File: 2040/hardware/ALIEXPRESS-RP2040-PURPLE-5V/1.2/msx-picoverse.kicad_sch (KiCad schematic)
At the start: 24 parts, among them Q1 BSS138, Q2 BSS138, Q3 BSS138, Q4 BSS138, Q5 BSS138, U1 RP2040-PURPLE

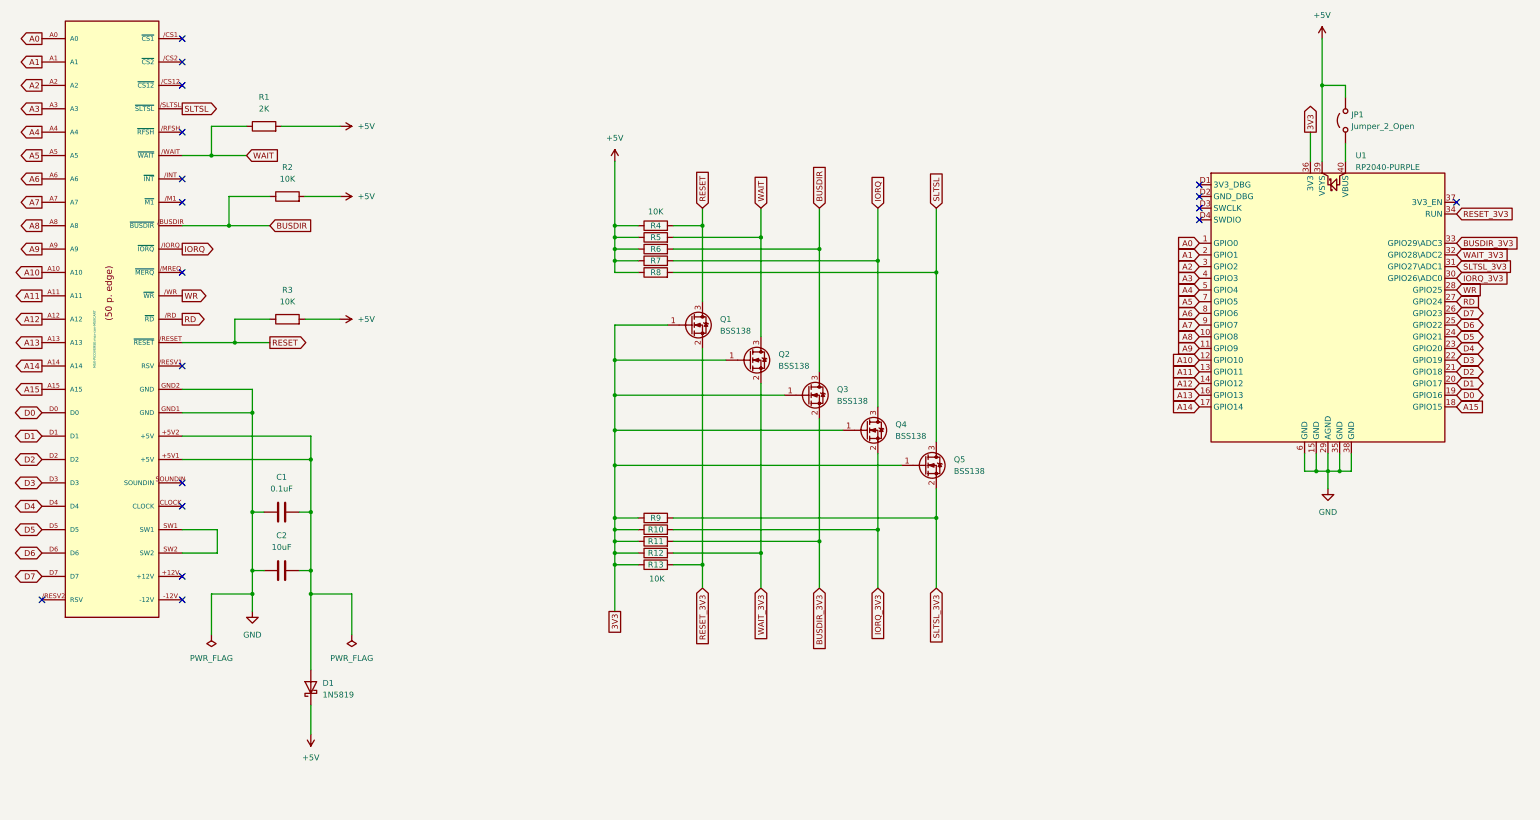
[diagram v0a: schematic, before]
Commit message: WiFi implementation for the 2040
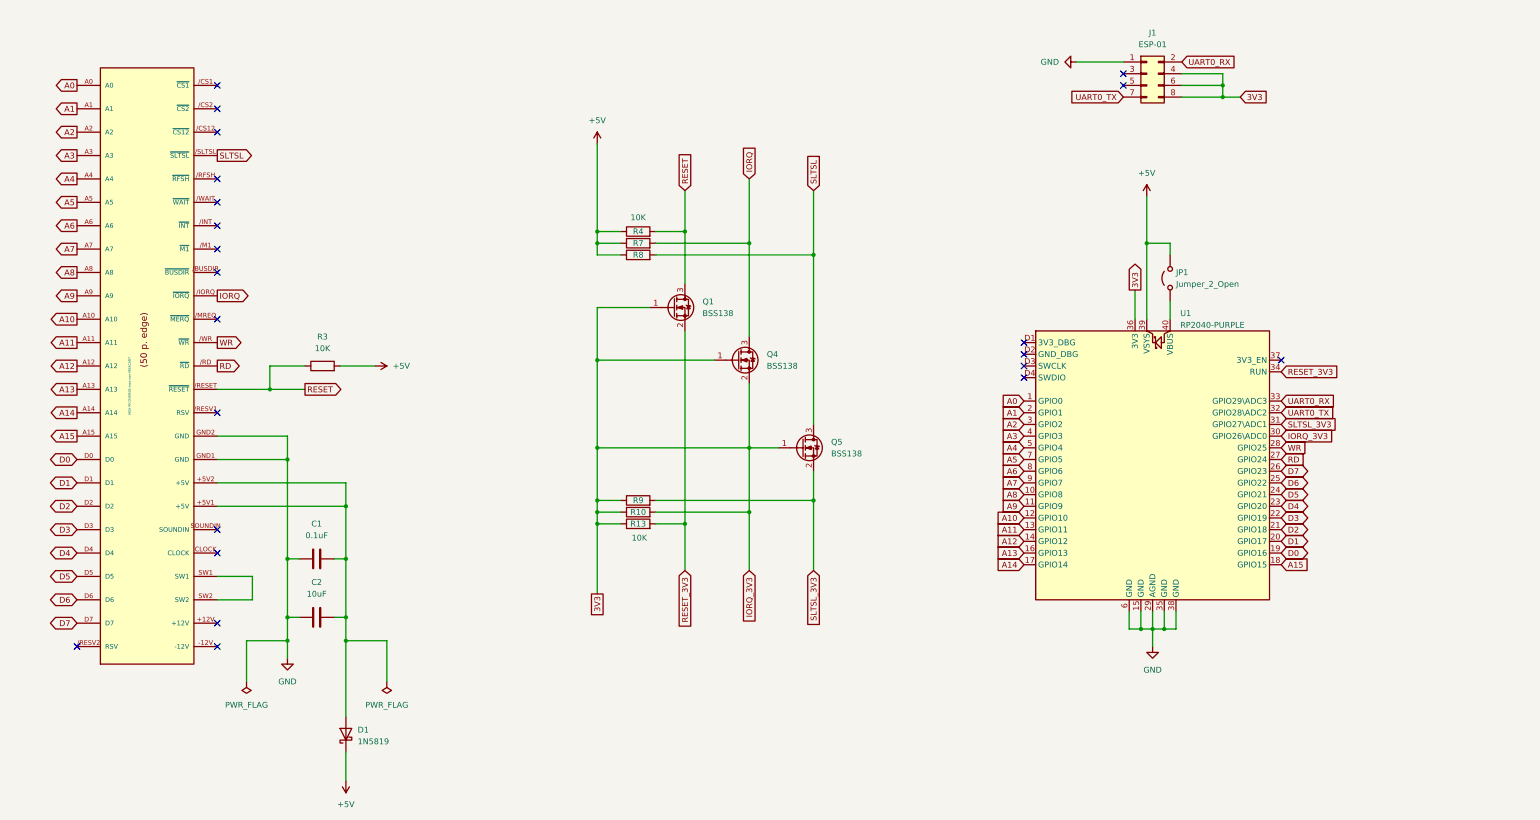
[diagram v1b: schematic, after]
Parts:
- removed Q2, Q3: BSS138, Package_TO_SOT_SMD:SOT-23, symbol Transistor_FET:BSS138
- removed R1: 2K, Resistor_SMD:R_0603_1608Metric_Pad0.98x0.95mm_HandSolder, symbol Device:R
- removed R11, R12, R2, R5, R6: 10K, Resistor_SMD:R_0603_1608Metric_Pad0.98x0.95mm_HandSolder, symbol Device:R
- added J1: ESP-01, Connector_PinSocket_2.54mm:PinSocket_2x04_P2.54mm_Vertical, symbol Connector_Generic:Conn_02x04_Odd_Even
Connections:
- net IORQ_3V3 is gone; now on net 3V3: Q4.2 (S), R10.2, U1.30 (GPIO26\ADC0)
- net 3V3: now also J1.4 (Pin_4), J1.6 (Pin_6), J1.8 (Pin_8)
- net GND: now also J1.1 (Pin_1)
- net BUSDIR: no longer names the net of EDG1./BUSDIR (~{BUSDIR})
- net BUSDIR_3V3 renamed UART0_RX
- net UART0_RX: now also J1.2 (Pin_2)
- net WAIT: no longer names the net of EDG1./WAIT (~{WAIT})
- net WAIT_3V3 renamed UART0_TX
- net UART0_TX: now also J1.7 (Pin_7)
- no-connect marks 18 -> 22
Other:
- moved on the sheet: C1, C2, D1, JP1, Q1, Q4, Q5, R10, R13, R3, R4, R7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

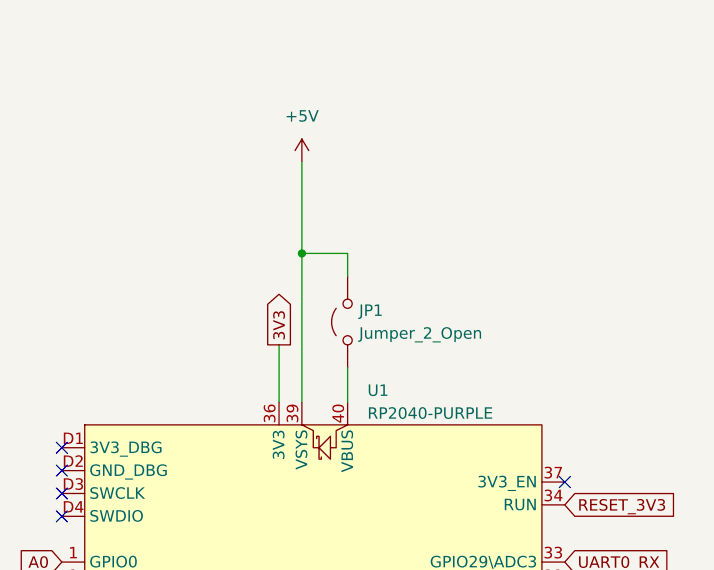
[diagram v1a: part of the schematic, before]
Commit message: ESP8266 on 2040
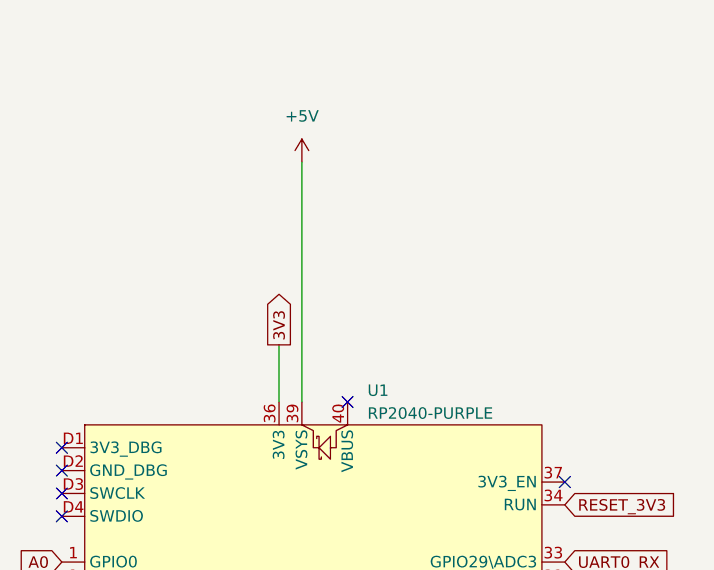
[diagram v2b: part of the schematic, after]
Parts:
- removed JP1: Jumper_2_Open, Jumper:SolderJumper-2_P1.3mm_Open_RoundedPad1.0x1.5mm, symbol Jumper:Jumper_2_Open
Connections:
- no-connect marks 22 -> 23
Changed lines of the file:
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@@
 	)
 	(junction
-		(at 312.42 110.49)
-		(diameter 0)
-		(color 0 0 0 0)
-	)
-	(junction
 		(at 328.93 76.2)
 		(diameter 0)
@@
 	)
 	(no_connect
+		(at 317.5 127)
+	)
+	(no_connect
 		(at 110.49 172.72)
 	)
@@
 	(wire
 		(pts
-			(xy 317.5 110.49) (xy 312.42 110.49)
-		)
-		(stroke
-			(width 0)
-			(type default)
-		)
-	)
-	(wire
-		(pts
 			(xy 138.43 179.07) (xy 138.43 191.77)
 		)
@@
 	(wire
 		(pts
-			(xy 317.5 123.19) (xy 317.5 127)
-		)
-		(stroke
-			(width 0)
-			(type default)
-		)
-	)
-	(wire
-		(pts
 			(xy 193.04 135.89) (xy 193.04 154.94)
 		)
@@
 	(wire
 		(pts
-			(xy 312.42 110.49) (xy 312.42 127)
-		)
-		(stroke
-			(width 0)
-			(type default)
-		)
-	)
-	(wire
-		(pts
-			(xy 317.5 113.03) (xy 317.5 110.49)
-		)
-		(stroke
-			(width 0)
-			(type default)
-		)
-	)
-	(wire
-		(pts
 			(xy 116.84 196.85) (xy 125.73 196.85)
 		)
@@
 	(wire
 		(pts
-			(xy 312.42 100.33) (xy 312.42 110.49)
+			(xy 312.42 100.33) (xy 312.42 127)
 		)
 		(stroke
@@
 					(unit 1)
 				)
-			)
-		)
-	)
-	(symbol
-		(lib_id "Jumper:Jumper_2_Open")
-		(at 317.5 118.11 90)
-		(unit 1)
-		(exclude_from_sim yes)
-		(in_bom yes)
-		(on_board yes)
-		(dnp no)
-		(fields_autoplaced yes)
-		(property "Reference" "JP1"
-			(at 318.77 116.8399 90)
-			(effects
-				(font
-					(size 1.27 1.27)
-				)
-				(justify right)
-			)
-		)
-		(property "Value" "Jumper_2_Open"
-			(at 318.77 119.3799 90)
-			(effects
-				(font
-					(size 1.27 1.27)
-				)
-				(justify right)
-			)
-		)
-		(property "Footprint" "Jumper:SolderJumper-2_P1.3mm_Open_RoundedPad1.0x1.5mm"
-			(at 317.5 118.11 0)
-			(effects
-				(font
-					(size 1.27 1.27)
-				)
-				(hide yes)
-			)
-		)
-		(property "Datasheet" "~"
-			(at 317.5 118.11 0)
-			(effects
-				(font
-					(size 1.27 1.27)
-				)
-				(hide yes)
-			)
-		)
-		(property "Description" "Jumper, 2-pole, open"
-			(at 317.5 118.11 0)
-			(effects
-				(font
-					(size 1.27 1.27)
-				)
-				(hide yes)
-			)
-		)
-		(pin "1"
-		)
-		(pin "2"
-		)
-		(instances
-			(project "msx-picoverse"
-				(path "/85986c19-ca47-44de-9ad3-96b5b9f34f81"
-					(reference "JP1")
-					(unit 1)
-				)
